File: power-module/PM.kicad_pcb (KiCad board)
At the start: 4 copper layers, 74.6 x 33.3 mm, 52 parts, among them J1 Conn_01x01, J2 Conn_01x04, J3 Conn_01x01, J4 Conn_01x16, U2 TAS5825MRHB

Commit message: wip
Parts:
- removed C26, C27, C28: 22n, Capacitor_SMD:C_0805_2012Metric
- removed FL3, FL4: PA2745NL, hw-footprints:PA2745NL
- added C36: 2n2, Capacitor_SMD:C_0603_1608Metric, F.Cu at (131.7, 95.0)
- added C37: 2n2, Capacitor_SMD:C_0603_1608Metric, F.Cu at (131.0, 79.2)
- added C38: 2n2, Capacitor_SMD:C_0603_1608Metric, F.Cu at (131.0, 76.5)
- added FB1: 50R@100MHz, Inductor_SMD:L_1206_3216Metric, F.Cu at (126.3, 96.5)
- added FB2: 50R@100MHz, Inductor_SMD:L_1206_3216Metric, F.Cu at (126.3, 90.3)
- added FB3: 50R@100MHz, Inductor_SMD:L_1206_3216Metric, F.Cu at (128.0, 73.5)
- added FB4: 50R@100MHz, Inductor_SMD:L_1206_3216Metric, F.Cu at (128.0, 78.5)
- added REF**: ESP32-S3-WROOM-1U, RF_Module:ESP32-S3-WROOM-1U, F.Cu at (210.6, 88.4)
- added REF**: ESP32-S3-WROOM-1, RF_Module:ESP32-S3-WROOM-1, F.Cu at (216.6, 54.8)
- C33: value 22n -> 2n2; footprint Capacitor_SMD:C_0805_2012Metric -> Capacitor_SMD:C_0603_1608Metric
- H1, H2, H3, H4: footprint MountingHole:MountingHole_3.2mm_M3_ISO14580_Pad -> MountingHole:MountingHole_2.7mm
- L6, L7: footprint hw-footprints:C2DEP1010 -> components:C2DEP1010
- moved N1 74.2 mm to (110.7, 84.7), turned to -90 degrees
- moved J3 38.9 mm to (173.7, 118.2)
- moved J1 34.7 mm to (173.6, 125.9)
- moved C6 15.6 mm to (125.6, 71.0)
- moved C5 15.6 mm to (123.3, 71.0)
- moved C22 14.9 mm to (124.0, 99.9)
- moved C24 14.9 mm to (124.0, 95.3)
- moved R5 14.9 mm to (124.0, 90.7)
- moved C25 14.5 mm to (124.5, 74.4), turned to 0 degrees
- moved C23 14.1 mm to (128.3, 100.7), turned to 0 degrees
- moved C4 13.6 mm to (129.1, 69.8), turned to 180 degrees
- moved R6 13.4 mm to (125.6, 78.6)
- moved H1 11.5 mm to (170.1, 71.2)
- moved H2 11.5 mm to (170.1, 99.6)
- moved C33 10.7 mm to (131.7, 92.0), turned to -90 degrees
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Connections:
- C33 pad 1: Net-(J2-Pin_2) -> Net-(J2-Pin_3)
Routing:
- net Net-(C17-Pad2): track 17.1 -> 0.00 mm
- net Net-(J2-Pin_1): track 7.90 -> 0.00 mm
- net Net-(J2-Pin_4): track 7.93 -> 1.10 mm
- net Net-(J2-Pin_2): track 6.81 -> 0.00 mm
- net Net-(J2-Pin_3): track 6.60 -> 0.00 mm
- net Net-(C20-Pad2): track 6.46 -> 0.00 mm
- net GND: track 54.1 -> 50.4 mm, vias 188 -> 108
- net Net-(C1-Pad1): track 0.00 -> 2.43 mm
- net Net-(C25-Pad1): track 0.00 -> 2.11 mm
- net Net-(U2-OUT_A-): track 6.15 -> 4.75 mm
- net Net-(C25-Pad2): track 1.69 -> 2.87 mm
- net Net-(U2-BST_B+): track 2.53 -> 1.79 mm
- net Net-(U2-BST_A+): track 2.56 -> 1.94 mm
- added copper zone on F.Cu, net Net-(J2-Pin_1)
- added copper zone on F.Cu, net Net-(J2-Pin_2)
- added copper zone on F.Cu, net Net-(J2-Pin_3)
- removed copper zone on F.Cu, net Net-(C20-Pad2)
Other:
- board size 74.6 x 33.3 mm -> 71.6 x 34.3 mm
- board text added: "L+"
- board text added: "L-"

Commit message: WIP
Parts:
- removed REF**: ESP32-S3-WROOM-1U, RF_Module:ESP32-S3-WROOM-1U
- removed REF**: ESP32-S3-WROOM-1, RF_Module:ESP32-S3-WROOM-1
- moved J1 44.4 mm to (166.6, 82.0), turned to 90 degrees
- moved J3 41.6 mm to (166.6, 77.2), turned to 90 degrees
- moved C5 11.5 mm to (133.9, 75.5), turned to -90 degrees
- moved C22 11.1 mm to (134.1, 95.2), turned to -90 degrees
- moved C24 7.75 mm to (131.7, 95.2)
- moved C25 7.18 mm to (131.6, 75.5), turned to -90 degrees
- moved C18 6.95 mm to (132.8, 86.7)
- moved C2 6.95 mm to (132.8, 84.3)
- moved C33 6.03 mm to (128.8, 86.8), turned to 0 degrees
- moved C6 5.98 mm to (131.6, 70.8)
- moved C36 5.60 mm to (126.2, 96.1), turned to 90 degrees
- moved C37 5.57 mm to (128.7, 84.3)
- moved R5 5.36 mm to (128.7, 93.1)
- moved FB2 5.34 mm to (131.6, 90.7), turned to 90 degrees
- moved C38 5.00 mm to (126.1, 75.8), turned to -90 degrees
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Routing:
- net GND: track 50.4 -> 38.6 mm, vias 108 -> 144
- net Net-(J2-Pin_2): track 0.00 -> 6.17 mm
- net Net-(J2-Pin_3): track 0.00 -> 5.82 mm
- net Net-(C1-Pad1): track 2.43 -> 0.00 mm
- net Net-(C25-Pad1): track 2.11 -> 0.00 mm
- net Net-(C24-Pad2): track 1.78 -> 3.30 mm
- net Net-(J2-Pin_4): track 1.10 -> 0.00 mm
- net Net-(C25-Pad2): track 2.87 -> 3.37 mm
- added copper zone on F.Cu, net Net-(C20-Pad2)
- added copper zone on F.Cu, net Net-(J2-Pin_4)
- removed copper zone on F.Cu, net Net-(J2-Pin_2)
- removed copper zone on F.Cu, net Net-(J2-Pin_3)
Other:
- board size 71.6 x 34.3 mm -> 65 x 34.3 mm

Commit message: wip
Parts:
- moved J3 4.90 mm to (164.7, 72.8)
- moved J1 4.66 mm to (164.4, 77.9)
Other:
- outline, holes or cut-outs redrawn
- board text removed: "C"
- board text removed: "D"

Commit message: WIP
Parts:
- moved J1 3.26 mm to (165.2, 74.8), turned to -90 degrees
- moved J3 1.95 mm to (165.3, 70.9)
- moved H2 0.98 mm to (172.3, 98.7)
- moved H4 0.97 mm to (113.0, 98.7)
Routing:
- net GND: vias 144 -> 152
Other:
- outline, holes or cut-outs redrawn

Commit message: WIP
TODO: Silk PM module. toslink module
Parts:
- added C26: 22u, Capacitor_SMD:C_0805_2012Metric, F.Cu at (157.5, 76.6)
- added C27: 22u, Capacitor_SMD:C_0805_2012Metric, F.Cu at (157.4, 94.4)
- moved J1 16.1 mm to (173.1, 88.8), turned to 0 degrees
- moved J3 13.1 mm to (173.1, 81.4), turned to 180 degrees
- moved C8 10.4 mm to (164.8, 74.1)
- moved C7 10.1 mm to (164.6, 97.0)
- moved C9 9.71 mm to (157.5, 78.6), turned to 180 degrees
- moved J4 9.61 mm to (165.1, 85.5)
- moved C10 9.47 mm to (157.4, 92.4), turned to 180 degrees
- moved R4 9.27 mm to (163.3, 81.2)
- moved C29 9.16 mm to (162.7, 82.7), turned to 0 degrees
- moved C13 9.07 mm to (156.1, 89.8)
- moved C15 9.07 mm to (156.1, 81.2)
- moved C1 9.07 mm to (147.5, 84.3)
- moved C11 9.07 mm to (158.9, 81.8)
- moved C12 9.07 mm to (158.8, 89.1)
- moved C14 9.07 mm to (151.8, 86.2)
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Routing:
- net /AMP_IO1: track 3.67 -> 4.94 mm
- net /AMP_IO2: track 3.69 -> 4.77 mm
- net Net-(U2-AVDD): track 2.81 -> 2.12 mm
- net /SDIN: track 3.08 -> 3.62 mm
- net /SCLK: track 3.08 -> 3.62 mm
- net /SDA: track 3.27 -> 3.81 mm
- net /LRCLK: track 3.30 -> 3.82 mm
- net GND: track 38.6 -> 38.5 mm, vias 152 -> 154
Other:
- board size 65 x 34.3 mm -> 66 x 34.3 mm

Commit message: RFM
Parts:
- moved C38 2.03 mm to (135.4, 73.0)
- moved C37 1.50 mm to (139.3, 84.3)
- moved C33 1.43 mm to (139.3, 86.8)
- moved C18 1.23 mm to (143.1, 86.7)
- moved C2 1.23 mm to (143.1, 84.3)
- moved J2 0.94 mm to (138.6, 85.4)
- moved C14 0.67 mm to (152.5, 86.2)
- moved C16 0.67 mm to (152.5, 84.7)
- moved C20 0.67 mm to (143.8, 99.9)
- moved C21 0.67 mm to (162.0, 90.1)
- moved C23 0.67 mm to (141.4, 99.9)
- moved C31 0.67 mm to (163.4, 87.8)
- moved C36 0.67 mm to (135.9, 96.1)
- moved C4 0.67 mm to (143.6, 70.8)
- moved C5 0.67 mm to (143.6, 75.5)
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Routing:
- net GND: track 38.5 -> 41.6 mm
- net +3V3: track 5.88 -> 6.42 mm
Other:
- outline, holes or cut-outs redrawn

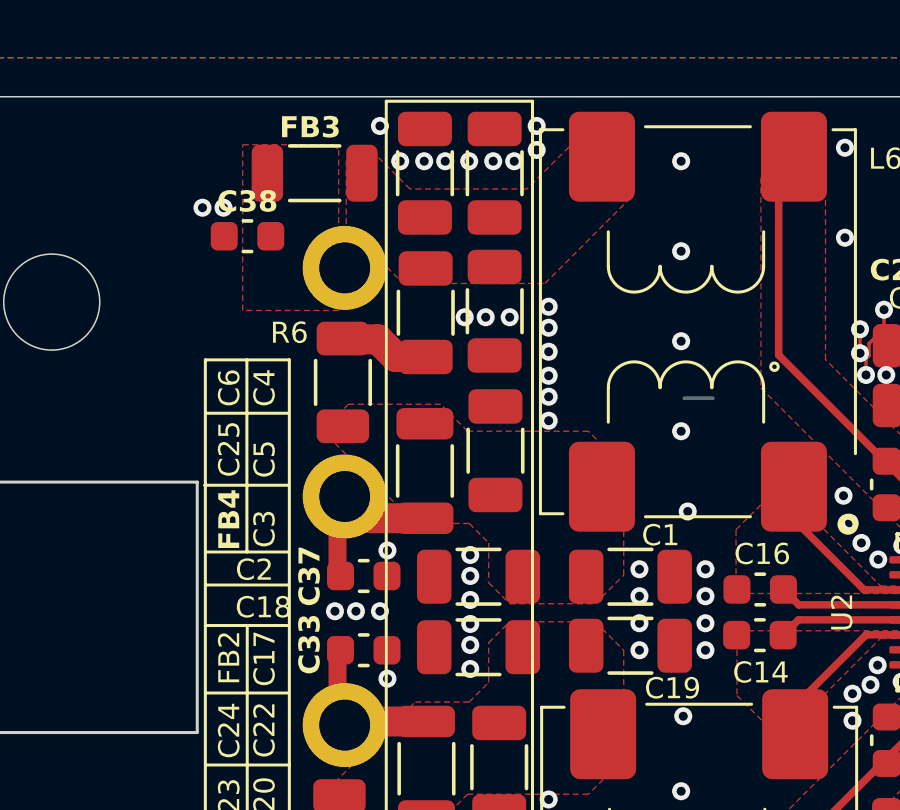
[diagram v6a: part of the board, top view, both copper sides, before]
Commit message: Adjusting outline optical reciever, fixing silkscreen errors
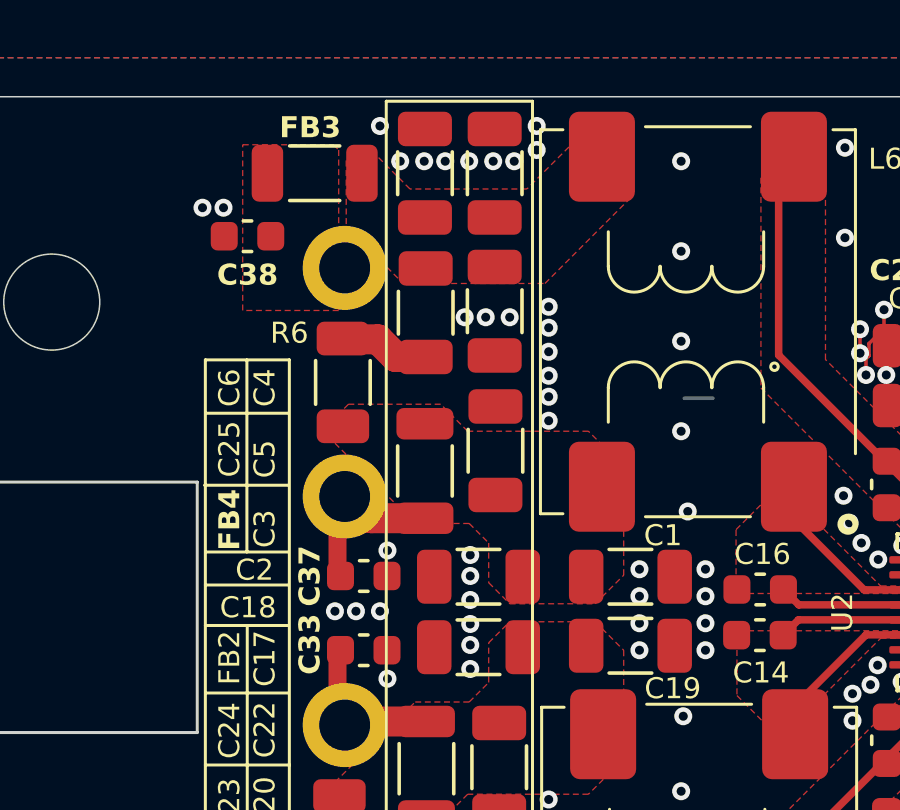
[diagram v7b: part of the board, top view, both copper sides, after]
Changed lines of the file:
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@@
 		(tags "capacitor")
 		(property "Reference" "C38"
-			(at 0 1.15 0)
+			(at 0 -1.29 0)
 			(layer "F.SilkS")
 			(effects
@@
 		(tags "capacitor")
 		(property "Reference" "C18"
-			(at -7.165 -1.323037 180)
+			(at -7.68 -1.323037 180)
 			(layer "F.SilkS")
 			(effects
@@
 		(tags "capacitor")
 		(property "Reference" "C1"
-			(at 1.01 -1.375 0)
+			(at 1.085 -1.375 0)
 			(layer "F.SilkS")
 			(effects

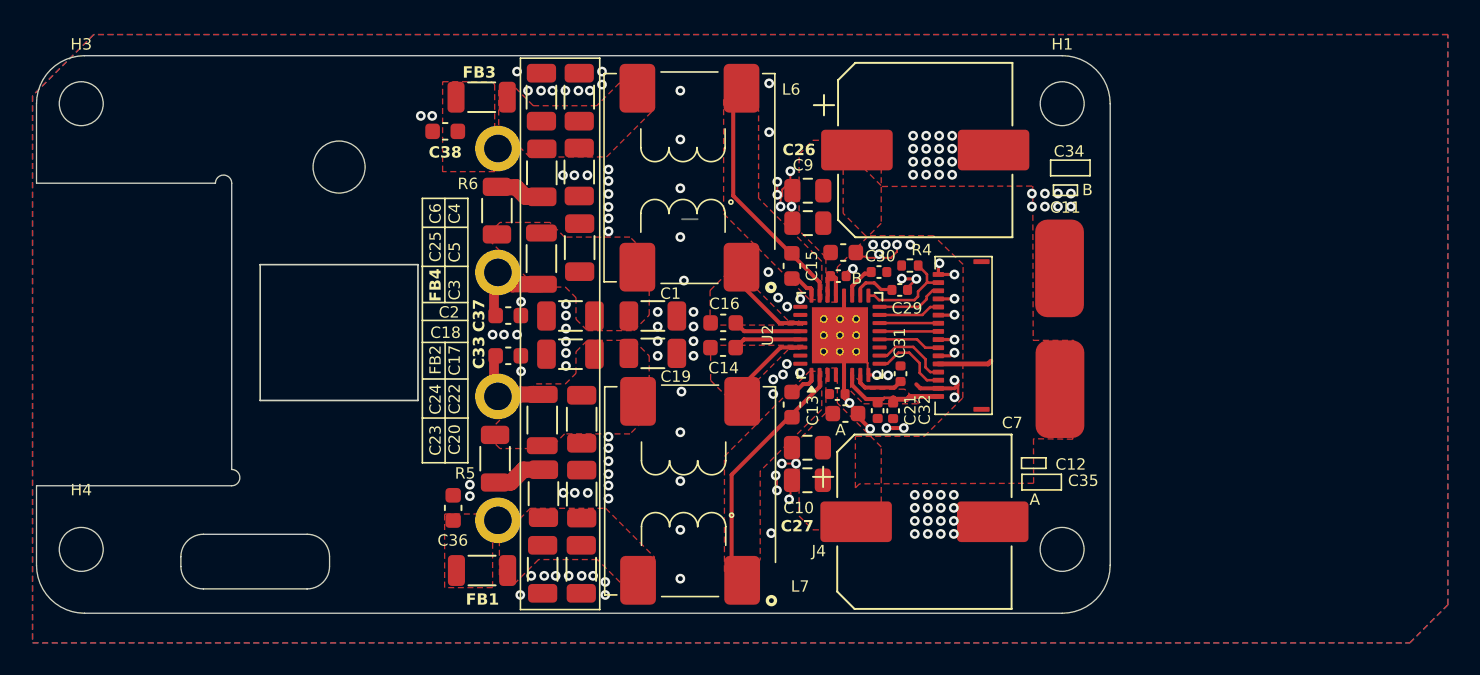
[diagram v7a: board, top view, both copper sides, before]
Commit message: JLC MPN fixes, minor tweaks
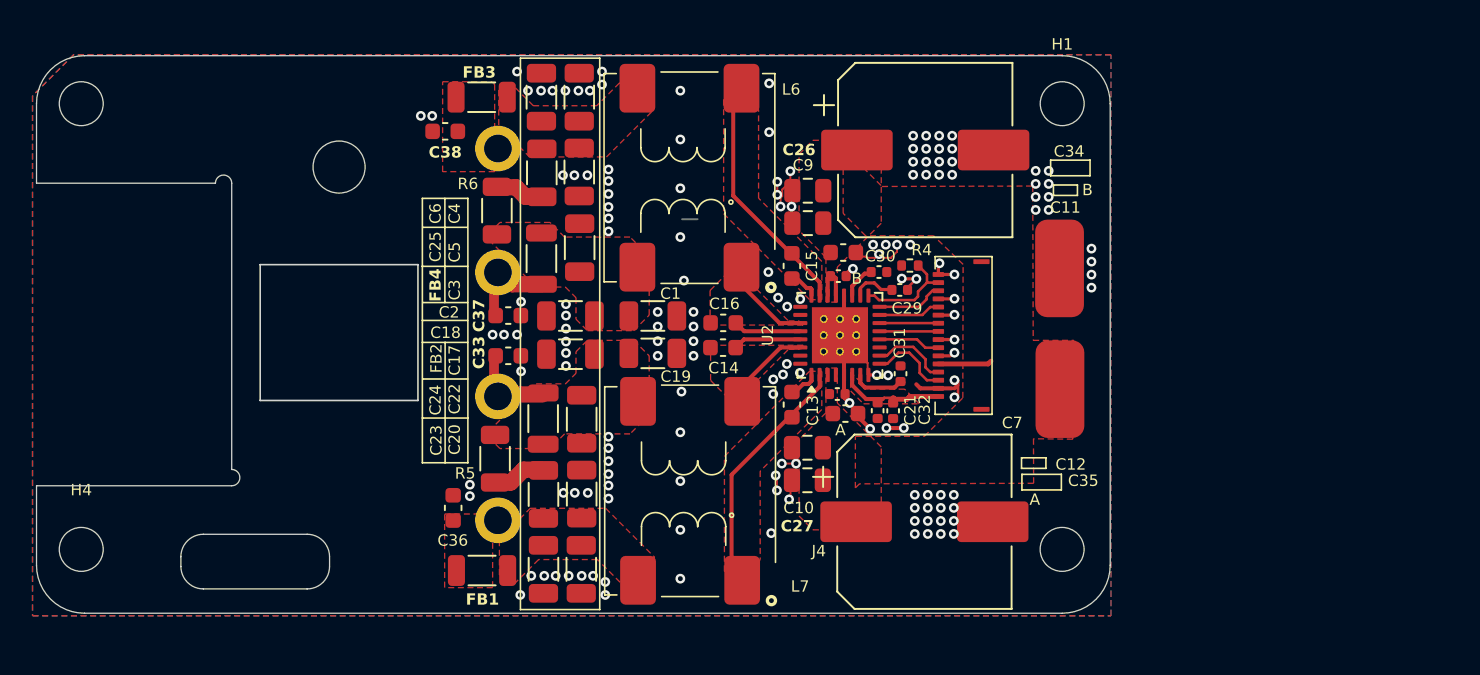
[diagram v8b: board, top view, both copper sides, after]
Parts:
- moved FB2 0.11 mm to (141.4, 90.6)
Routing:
- net GND: vias 154 -> 158
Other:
- board text added: "R+"
- board text added: "R-"
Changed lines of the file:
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@@
 			(at 0 -3.65 0)
 			(layer "F.SilkS")
+			(hide yes)
 			(effects
 				(font
@@
 	(footprint "Inductor_SMD:L_1206_3216Metric"
 		(layer "F.Cu")
-		(at 141.37 90.7 90)
+		(at 141.425 90.61 90)
 		(descr "Inductor SMD 1206 (3216 Metric), square (rectangular) end terminal, IPC-7351 nominal, (Body size source: IPC-SM-782 page 80, https://www.pcb-3d.com/wordpress/wp-content/uploads/ipc-sm-782a_amendment_1_and_2.pdf)")
 		(tags "inductor")
@@
 			)
 		)
-		(attr smd dnp)
+		(attr smd)
 		(duplicate_pad_numbers_are_jumpers no)
 		(fp_line
@@
 			)
 		)
-		(attr smd dnp)
+		(attr smd)
 		(duplicate_pad_numbers_are_jumpers no)
 		(fp_line
@@
 	(footprint "Capacitor_SMD:C_1206_3216Metric"
 		(layer "F.Cu")
-		(at 141.445 95.225 90)
+		(at 141.445 95.27 90)
 		(descr "Capacitor SMD 1206 (3216 Metric), square (rectangular) end terminal, IPC-7351 nominal, (Body size source: IPC-SM-782 page 76, https://www.pcb-3d.com/wordpress/wp-content/uploads/ipc-sm-782a_amendment_1_and_2.pdf)")
 		(tags "capacitor")
@@
 	(footprint "Capacitor_SMD:C_1206_3216Metric"
 		(layer "F.Cu")
-		(at 141.395 99.875 90)
+		(at 141.445 99.875 90)
 		(descr "Capacitor SMD 1206 (3216 Metric), square (rectangular) end terminal, IPC-7351 nominal, (Body size source: IPC-SM-782 page 76, https://www.pcb-3d.com/wordpress/wp-content/uploads/ipc-sm-782a_amendment_1_and_2.pdf)")
 		(tags "capacitor")
@@
 	)
 	(gr_text "L+"
-		(at 144.659103 74.799475 0)
+		(at 153.585 74.799475 0)
 		(layer "B.SilkS")
 		(effects
@@
 	)
 	(gr_text "L-"
-		(at 144.659103 80.95 0)
+		(at 153.585 82.63 0)
 		(layer "B.SilkS")
 		(effects
@@
 		)
 	)
-	(gr_text "L+"
-		(at 144.659103 85.25 0)
+	(gr_text "R-"
+		(at 153.585 90.23 0)
 		(layer "B.SilkS")
 		(effects
@@
 		)
 	)
-	(gr_text "L+"
-		(at 144.659103 89.05 0)
+	(gr_text "R+"
+		(at 153.585 98.02 0)
 		(layer "B.SilkS")
 		(effects
@@
 	)
 	(gr_text "Legion RT-C08-M2-BJ"
-		(at 171.085 63.25 0)
+		(at 108.175 98.18 90)
 		(layer "Cmts.User")
 		(effects
@@
 	)
 	(via
+		(at 175.135 82.56)
+		(size 0.6)
+		(drill 0.3)
+		(layers "F.Cu" "B.Cu")
+		(net "GND")
+	)
+	(via
 		(at 165.7725 74.02)
 		(size 0.6)
@@
 	)
 	(via
+		(at 175.135 81.76)
+		(size 0.6)
+		(drill 0.3)
+		(layers "F.Cu" "B.Cu")
+		(net "GND")
+	)
+	(via
 		(at 145.445 78.3)
 		(size 0.6)
@@
 	)
 	(via
-		(at 173.0725 76.775)
+		(at 172.505 76.98)
+		(size 0.6)
+		(drill 0.3)
+		(layers "F.Cu" "B.Cu")
+		(net "GND")
+	)
+	(via
+		(at 175.135 80.96)
 		(size 0.6)
 		(drill 0.3)
@@
 	)
 	(via
-		(at 173.0725 77.575)
+		(at 171.705 76.98)
 		(size 0.6)
 		(drill 0.3)
@@
 	)
 	(via
-		(at 172.2725 77.575)
+		(at 171.705 76.18)
 		(size 0.6)
 		(drill 0.3)
@@
 	)
 	(via
-		(at 173.8725 76.775)
+		(at 172.505 77.78)
 		(size 0.6)
 		(drill 0.3)
@@
 	)
 	(via
-		(at 171.4725 76.775)
+		(at 172.505 75.38)
 		(size 0.6)
 		(drill 0.3)
@@
 	)
 	(via
+		(at 175.135 80.16)
+		(size 0.6)
+		(drill 0.3)
+		(layers "F.Cu" "B.Cu")
+		(net "GND")
+	)
+	(via
 		(at 165.7725 73.22)
 		(size 0.6)
@@
 	)
 	(via
-		(at 171.4725 77.575)
+		(at 171.705 75.38)
 		(size 0.6)
 		(drill 0.3)
@@
 	)
 	(via
-		(at 172.2725 76.775)
+		(at 172.505 76.18)
 		(size 0.6)
 		(drill 0.3)
@@
 	)
 	(via
-		(at 173.8725 77.575)
+		(at 171.705 77.78)
 		(size 0.6)
 		(drill 0.3)
@@
 		(polygon
 			(pts
-				(xy 110.035 70.765) (xy 110.035 104.4) (xy 194.7 104.4) (xy 197.05 102.05) (xy 197.05 67) (xy 113.8 67)
+				(xy 110.035 70.765) (xy 110.035 102.73) (xy 176.335 102.73) (xy 176.335 68.24) (xy 112.56 68.24)
 			)
 		)
